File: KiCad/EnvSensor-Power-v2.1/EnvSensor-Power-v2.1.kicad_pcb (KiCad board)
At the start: 4 copper layers, 102 x 100 mm, 146 parts, among them J1 USB_B_Micro, J2 USB_C_Receptacle_USB2.0, J3 BattSense, J4 3V3 Sense, J5 5V Sense, J6 POWER_OUTPUT, Q1 AO6804A, Q2 ZXMP6A16K, SW1 BATT_SWITCH, SW2 Start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

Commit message: Finish
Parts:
- added C47: Cx, Capacitor_SMD:C_0805_2012Metric, B.Cu at (74.8, 87.0)
- added C48: Cx, Capacitor_SMD:C_0805_2012Metric, B.Cu at (74.8, 101.6)
- added C49: Cx, Capacitor_SMD:C_0805_2012Metric, B.Cu at (47.0, 59.4)
- added C50: Cx, Capacitor_SMD:C_0805_2012Metric, B.Cu at (47.0, 79.2)
- added R32: Rx, Resistor_SMD:R_0805_2012Metric, B.Cu at (72.0, 88.0)
- added R33: Rx, Resistor_SMD:R_0805_2012Metric, B.Cu at (72.0, 102.6)
- added R34: Rx, Resistor_SMD:R_0805_2012Metric, B.Cu at (44.2, 60.2)
- added R35: Rx, Resistor_SMD:R_0805_2012Metric, B.Cu at (44.2, 80.0)
- added TS10: TestPoint, TestPoint:TestPoint_THTPad_D1.5mm_Drill0.7mm, B.Cu at (74.8, 92.0)
- added TS11: TestPoint, TestPoint:TestPoint_THTPad_D1.5mm_Drill0.7mm, B.Cu at (89.6, 97.2)
- added TS12: TestPoint, TestPoint:TestPoint_THTPad_D1.5mm_Drill0.7mm, B.Cu at (74.8, 106.0)
- added TS13: TestPoint, TestPoint:TestPoint_THTPad_D1.5mm_Drill0.7mm, B.Cu at (91.2, 83.4)
- added TS14: TestPoint, TestPoint:TestPoint_THTPad_D1.5mm_Drill0.7mm, B.Cu at (73.4, 61.2)
- added TS15: TestPoint, TestPoint:TestPoint_THTPad_D1.5mm_Drill0.7mm, B.Cu at (74.8, 75.6)
- added TS9: TestPoint, TestPoint:TestPoint_THTPad_D1.5mm_Drill0.7mm, B.Cu at (50.6, 88.4)
- moved TS3 15.6 mm to (72.2, 78.2)
- moved TS8 4.60 mm to (74.8, 97.2)
- moved TS5 2.41 mm to (74.8, 83.2)
- moved C35 1.40 mm to (76.8, 101.6)
- moved C44 1.34 mm to (49.0, 79.2)
- moved C14 1.30 mm to (76.8, 87.0)
- moved C18 1.25 mm to (49.0, 59.4)
- moved C17 0.80 mm to (41.5, 59.4)
- moved L3 0.80 mm to (44.2, 58.4)
- moved C43 0.76 mm to (41.4, 79.2)
- moved C13 0.75 mm to (69.2, 87.0)
- moved L2 0.75 mm to (72.0, 86.0)
- moved L7 0.71 mm to (44.2, 78.2)
- moved L6 0.71 mm to (71.9, 100.7)
- moved C34 0.71 mm to (69.2, 101.6)
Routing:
- net GND: track 154.2 -> 161.8 mm, vias 65 -> 69
- net /5V_REG: track 17.0 -> 19.9 mm
- net /3V7_NOT_REG: track 79.8 -> 77.9 mm
- net Net-(C50-Pad2): track 0.00 -> 1.95 mm
- net Net-(C49-Pad2): track 0.00 -> 1.95 mm
- net Net-(C48-Pad2): track 0.00 -> 1.91 mm
- net Net-(C47-Pad2): track 0.00 -> 1.91 mm
- net /5V5_FILTERED: track 11.8 -> 13.5 mm
- net /5V_IN: track 20.6 -> 21.9 mm
- net /BATT_3V3_FILTER: track 71.5 -> 72.5 mm
- net +BATT: track 204.9 -> 205.9 mm
- net /5V5_NOT_REG: track 27.6 -> 27.0 mm
- net /3V3_FILTER: track 11.8 -> 12.5 mm
- net VBUS: track 265.9 -> 265.2 mm
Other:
- board text added: "EnvSensor 2.1 Power Supply JP, 22.07.2024 Wrocław"
- board text added: "GND"
- board text removed: "EnvSensor 2.1 Power Supply JP, 8.04.2023"

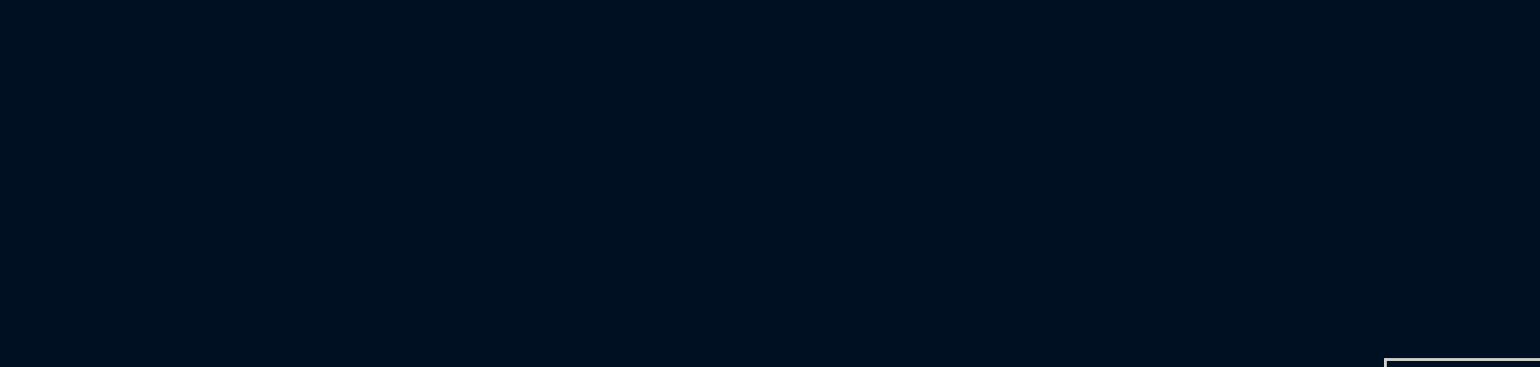
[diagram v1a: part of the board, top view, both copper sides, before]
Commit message: c++ project for 2.1 introduced
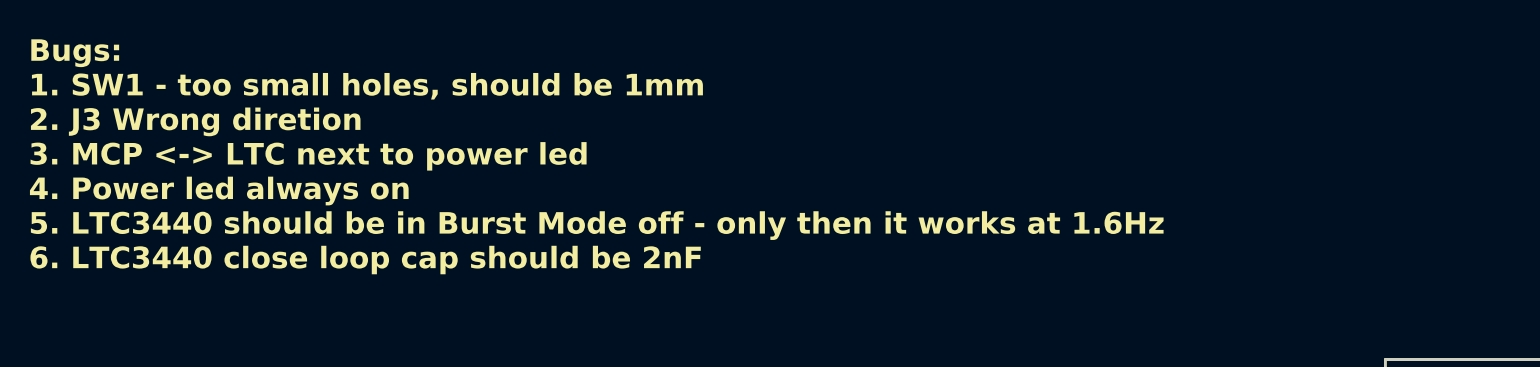
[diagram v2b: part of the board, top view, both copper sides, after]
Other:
- board text added: "Bugs: 1. SW1 - too small holes, should be 1mm 2. J3 Wrong diretion 3. MCP <-> LTC next to power led 4. Power led always on 5. LTC3440 should be in Burst Mode off - only then it works at 1.6Hz 6. LTC3440 close loop cap should be 2nF"
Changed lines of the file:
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@@
     (effects (font (size 1.5 1.5) (thickness 0.2)) (justify left))
+  )
+  (gr_text "Bugs:\n1. SW1 - too small holes, should be 1mm\n2. J3 Wrong diretion\n3. MCP <-> LTC next to power led\n4. Power led always on\n5. LTC3440 should be in Burst Mode off - only then it works at 1.6Hz\n6. LTC3440 close loop cap should be 2nF" (at -74.8 13.8) (layer "F.SilkS")
+    (effects (font (size 1.5 1.5) (thickness 0.3) bold) (justify left bottom))
   )
   (gr_text "Keep Out" (at 111 55 90) (layer "F.SilkS")
